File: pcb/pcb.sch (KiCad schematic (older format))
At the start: 31 parts, among them J1 Conn_01x10, J2 Conn_01x06, J3 Conn_01x06, J4 Conn_01x06, J5 Conn_01x06, J6 Conn_01x06, J7 Conn_01x06, J8 Conn_01x10, U1 teensy-2.0

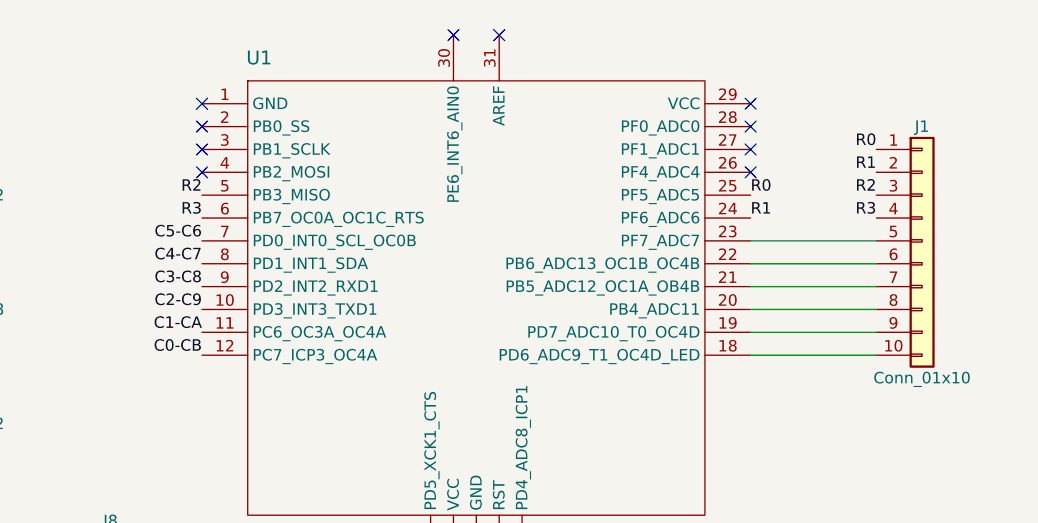
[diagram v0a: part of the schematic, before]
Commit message: Change pin for column B to avoid teensy LED
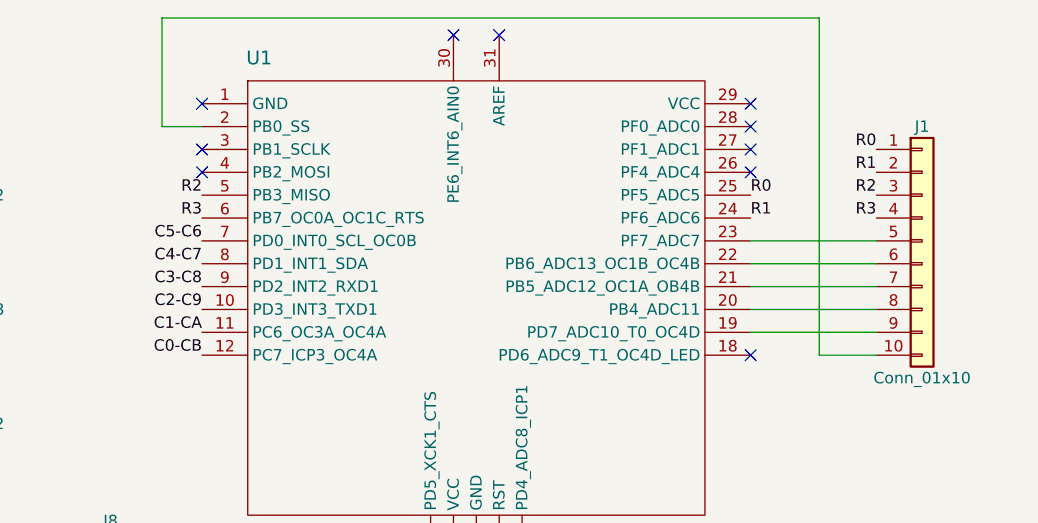
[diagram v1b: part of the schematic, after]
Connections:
- net at U1.18 (PD6_ADC9_T1_OC4D_LED): no longer J1.10 (Pin_10)
- net at U1.2 (PB0_SS): now also J1.10 (Pin_10)
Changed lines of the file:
@@
 NoConn ~ 6300 1300
 NoConn ~ 6300 1200
-NoConn ~ 6300 1100
+NoConn ~ 8700 2100
 NoConn ~ 6300 1000
 NoConn ~ 7400 700
@@
 $EndComp
 Wire Wire Line
-	9250 2100 8700 2100
-Wire Wire Line
 	9250 2000 8700 2000
 Wire Wire Line
@@
 Wire Wire Line
 	9750 6150 9750 6250
+Wire Wire Line
+	9250 2100 9000 2100
+Wire Wire Line
+	9000 2100 9000 625
+Wire Wire Line
+	9000 625  6125 625
+Wire Wire Line
+	6125 625  6125 1100
+Wire Wire Line
+	6125 1100 6300 1100
 $EndSCHEMATC

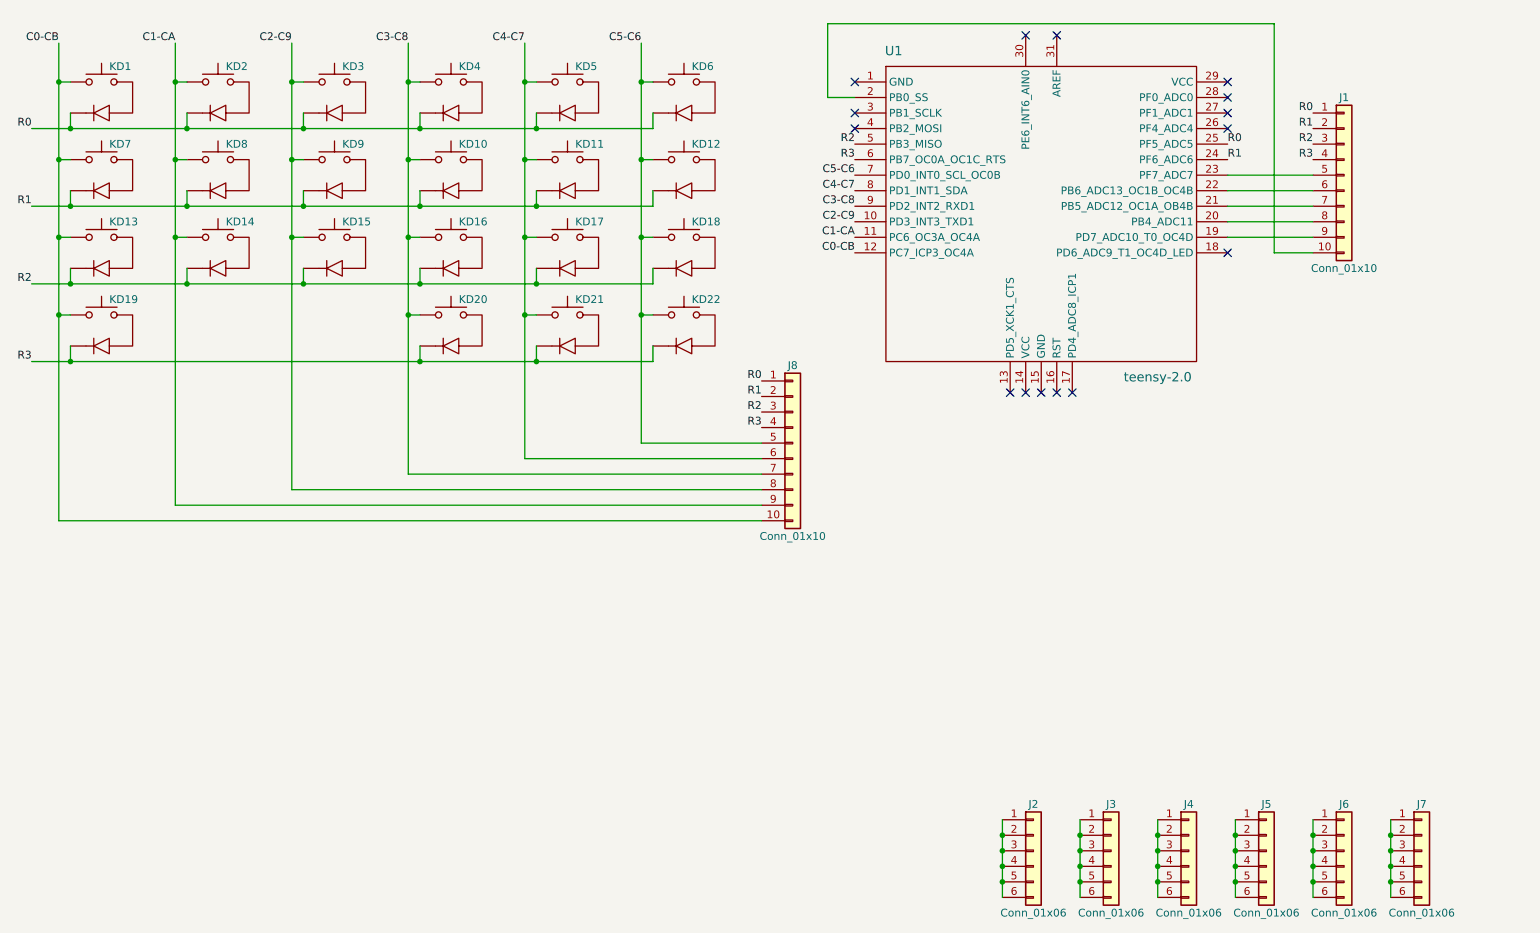
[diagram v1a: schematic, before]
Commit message: Use single IDC header and prep outline for magnets
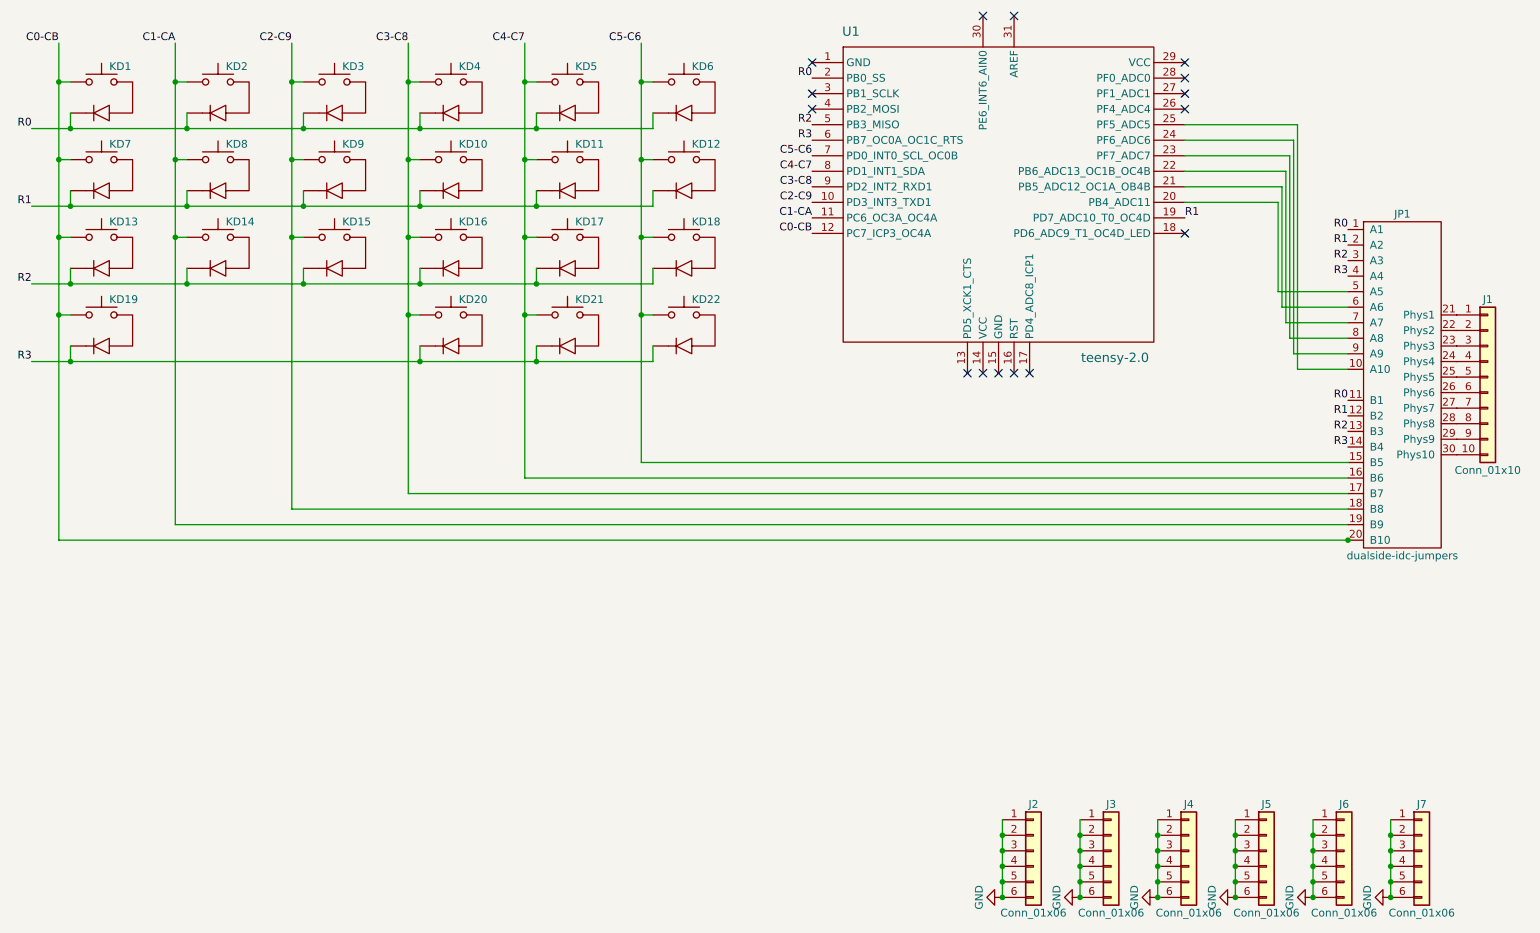
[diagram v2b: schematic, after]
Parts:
- removed J8: Conn_01x10, keyboard-parts:idc-header_2x05_2.54mm, symbol Connector_Generic:Conn_01x10
- added JP1: dualside-idc-jumpers, keyboard-parts:dualside-idc-jumpers, symbol keyboard-parts:dualside-idc-jumpers
- J1: footprint keyboard-parts:idc-header_2x05_2.54mm -> keyboard-parts:idc-header-dualside_2x05_2.54mm
- J2, J3, J4, J5, J6, J7: footprint keyboard-parts:header_1x06_2.54mm -> keyboard-parts:header_sym_1x06_2.54mm
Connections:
- net C0-CB: now also JP1.20 (B10)
- net C1-CA: now also JP1.19 (B9)
- net C2-C9: now also JP1.18 (B8)
- net C3-C8: now also JP1.17 (B7)
- net C4-C7: now also JP1.16 (B6)
- net C5-C6: now also JP1.15 (B5)
- net R0: now also U1.2 (PB0_SS), JP1.1 (A1), JP1.11 (B1); no longer J1.1 (Pin_1), U1.25 (PF5_ADC5)
- net R1: now also U1.19 (PD7_ADC10_T0_OC4D), JP1.12 (B2), JP1.2 (A2); no longer J1.2 (Pin_2), U1.24 (PF6_ADC6)
- net R2: now also JP1.13 (B3), JP1.3 (A3); no longer J1.3 (Pin_3)
- net R3: now also JP1.14 (B4), JP1.4 (A4); no longer J1.4 (Pin_4)
- net at J1.9 (Pin_9): now also JP1.29 (Phys9); no longer U1.19 (PD7_ADC10_T0_OC4D)
- net at J1.10 (Pin_10): now also JP1.30 (Phys10); no longer U1.2 (PB0_SS)
- net at U1.20 (PB4_ADC11): now also JP1.5 (A5); no longer J1.8 (Pin_8)
- net at U1.21 (PB5_ADC12_OC1A_OB4B): now also JP1.6 (A6); no longer J1.7 (Pin_7)
- net at U1.22 (PB6_ADC13_OC1B_OC4B): now also JP1.7 (A7); no longer J1.6 (Pin_6)
- net at U1.23 (PF7_ADC7): now also JP1.8 (A8); no longer J1.5 (Pin_5)
- net GND: now reaches J2.1 (Pin_1), J2.2 (Pin_2), J2.3 (Pin_3), J2.4 (Pin_4), J2.5 (Pin_5), J2.6 (Pin_6)
- net GND: now also J3.1 (Pin_1), J3.2 (Pin_2), J3.3 (Pin_3), J3.4 (Pin_4), J3.5 (Pin_5), J3.6 (Pin_6), J4.1 (Pin_1), J4.2 (Pin_2), J4.3 (Pin_3), J4.4 (Pin_4), J4.5 (Pin_5), J4.6 (Pin_6), J5.1 (Pin_1), J5.2 (Pin_2), J5.3 (Pin_3), J5.4 (Pin_4), J5.5 (Pin_5), J5.6 (Pin_6), J6.1 (Pin_1), J6.2 (Pin_2), J6.3 (Pin_3), J6.4 (Pin_4), J6.5 (Pin_5), J6.6 (Pin_6), J7.1 (Pin_1), J7.2 (Pin_2), J7.3 (Pin_3), J7.4 (Pin_4), J7.5 (Pin_5), J7.6 (Pin_6)
- new net: JP1.9 (A9), U1.24 (PF6_ADC6)
- new net: JP1.10 (A10), U1.25 (PF5_ADC5)
- new net: J1.1 (Pin_1), JP1.21 (Phys1)
- new net: J1.2 (Pin_2), JP1.22 (Phys2)
- new net: J1.3 (Pin_3), JP1.23 (Phys3)
- new net: J1.4 (Pin_4), JP1.24 (Phys4)
- new net: J1.5 (Pin_5), JP1.25 (Phys5)
- new net: J1.6 (Pin_6), JP1.26 (Phys6)
- new net: J1.7 (Pin_7), JP1.27 (Phys7)
- new net: J1.8 (Pin_8), JP1.28 (Phys8)
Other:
- moved on the sheet: J1, U1
